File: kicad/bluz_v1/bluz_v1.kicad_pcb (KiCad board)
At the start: 2 copper layers, 24.9 x 14.9 mm, 70 parts, among them J1 USB_B_Micro, J10 Conn, J11 Conn, J12 BTAnt, J2 Conn, J3 Conn, J4 Conn, J5 Conn, J6 Conn, J7 Conn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

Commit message: изменено:      kicad/bluz_v1/bluz_v1.kicad_pcb 	изменено:      kicad/bluz_v1/bluz_v1.kicad_prl 	изменено:      kicad/bluz_v1/bluz_v1.kicad_sch
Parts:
- moved D3 0.78 mm to (80.9, 43.3), turned to 180 degrees
- moved J3 0.16 mm to (82.5, 45.1)
- moved R5 0.09 mm to (82.9, 43.6)
- moved R2 0.09 mm to (81.3, 44.8)
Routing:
- net GND: track 180.8 -> 204.5 mm
- net Net-(D3-Pad1): track 2.48 -> 1.03 mm
- net LED: track 2.35 -> 2.86 mm

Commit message: изменено:      kicad/bluz_v1/bluz_v1.kicad_pcb 	изменено:      kicad/bluz_v1/bluz_v1.kicad_sch 	изменено:      kicad/bluz_v1/fp-info-cache
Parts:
- C12: value .1 -> 10n
- C16: footprint Capacitor_SMD:C_0805_2012Metric -> Capacitor_SMD:C_1206_3216Metric
- C19: footprint Capacitor_SMD:C_0805_2012Metric -> Capacitor_SMD:C_1206_3216Metric; moved to B.Cu
- J11: moved to B.Cu
- moved C19 3.86 mm to (68.0, 40.0), turned to 90 degrees
- moved J11 3.26 mm to (66.3, 38.6)
- moved R14 1.57 mm to (69.7, 38.3), turned to 180 degrees
- moved C16 1.14 mm to (69.9, 41.0)
- moved J10 0.40 mm to (69.6, 42.4)
- moved J6 0.35 mm to (66.2, 49.9)
- moved D5 0.35 mm to (67.7, 41.8)
- moved R15 0.23 mm to (66.2, 38.4)
- moved R13 0.22 mm to (67.6, 38.0)
- moved J12 0.15 mm to (70.6, 39.3)
- moved R16 0.12 mm to (68.2, 39.4)
- moved C9 0.11 mm to (67.3, 39.4)
- moved J3 0.07 mm to (82.6, 45.0)
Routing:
- net GND: track 204.5 -> 208.7 mm
- net Net-(C16-Pad2): track 5.68 -> 6.97 mm
- net /+SiPM: track 2.65 -> 3.01 mm, vias 0 -> 1

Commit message: изменено:      kicad/bluz_v1/bluz_v1.kicad_pcb 	изменено:      kicad/bluz_v1/bluz_v1.kicad_sch 	изменено:      stm32cubeide/BluZ_v1/.cproject 	изменено:      stm32cubeide/BluZ_v1/.mxproject 	изменено:      stm32cubeide/BluZ_v1/.settings/language.settings.xml 	изменено:      stm32cubeide/BluZ_v1/BluZ_v1.ioc 	изменено:      stm32cubeide/BluZ_v1/Core/Inc/app_conf.h 	изменено:      stm32cubeide/BluZ_v1/Core/Inc/main.h 	изменено:      stm32cubeide/BluZ_v1/Core/Inc/stm32wbaxx_it.h 	изменено:      stm32cubeide/BluZ_v1/Core/Src/app_entry.c 	изменено:      stm32cubeide/BluZ_v1/Core/Src/main.c 	изменено:      stm32cubeide/BluZ_v1/Core/Src/stm32wbaxx_hal_msp.c 	изменено:      stm32cubeide/BluZ_v1/Core/Src/stm32wbaxx_it.c
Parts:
- D4: value LTC1661CMS8 -> LTC1662CMS8
- L1: value 47uH -> 10uH
- Q1, Q2, R11, R12: moved to B.Cu
- moved R11 10.8 mm to (83.7, 48.6), turned to 0 degrees
- moved Q1 10.5 mm to (83.5, 50.2)
- moved R12 5.25 mm to (85.0, 45.4), turned to 0 degrees
- moved J9 4.24 mm to (72.3, 47.3)
- moved J4 4.17 mm to (73.3, 48.3)
- moved J5 3.06 mm to (74.5, 47.9)
- moved Q2 2.84 mm to (84.9, 46.9), turned to -90 degrees
- moved L1 2.08 mm to (78.5, 41.8), turned to -90 degrees
- moved J2 1.47 mm to (70.2, 41.5)
- moved C18 1.09 mm to (71.3, 40.9), turned to -90 degrees
- moved R1 0.90 mm to (80.6, 44.7), turned to 90 degrees
- moved J10 0.77 mm to (69.2, 43.0)
- moved BZ1 0.49 mm to (78.3, 48.6)
- moved R2 0.30 mm to (81.6, 44.7)
- moved C11 0.26 mm to (83.1, 42.7)
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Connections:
- D1 pad 15: Sound -> unconnected-(D1-Pad15)
- D1 pad 17: Sync -> unconnected-(D1-Pad17)
- D1 pad 21: unconnected-(D1-Pad21) -> Sync
- D1 pad 6: unconnected-(D1-Pad6) -> LED
- D1 pad 7: LED -> batLev
- D1 pad 8: batLev -> Sound
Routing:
- net GND: track 208.7 -> 203.0 mm
- net Sound: track 4.47 -> 8.57 mm, vias 1 -> 2
- net Sync: track 10.5 -> 14.6 mm
- net /swd: track 1.93 -> 5.88 mm
- net /TxD: track 1.91 -> 5.37 mm
- net Vibro: track 13.9 -> 10.6 mm, vias 1 -> 2
- net Net-(BZ1-Pad2): track 7.86 -> 4.86 mm, vias 0 -> 1
- net /swc: track 2.18 -> 4.97 mm
- net Net-(M1-Pad1): track 1.81 -> 0.00 mm, vias 0 -> 1
- net +BATT: track 37.0 -> 38.6 mm
- net Net-(C23-Pad1): track 4.22 -> 5.44 mm

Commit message: изменено:      kicad/bluz_v1/bluz_v1.kicad_pcb 	изменено:      kicad/bluz_v1/bluz_v1.kicad_prl 	изменено:      kicad/bluz_v1/fp-info-cache
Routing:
- net GND: vias 18 -> 19

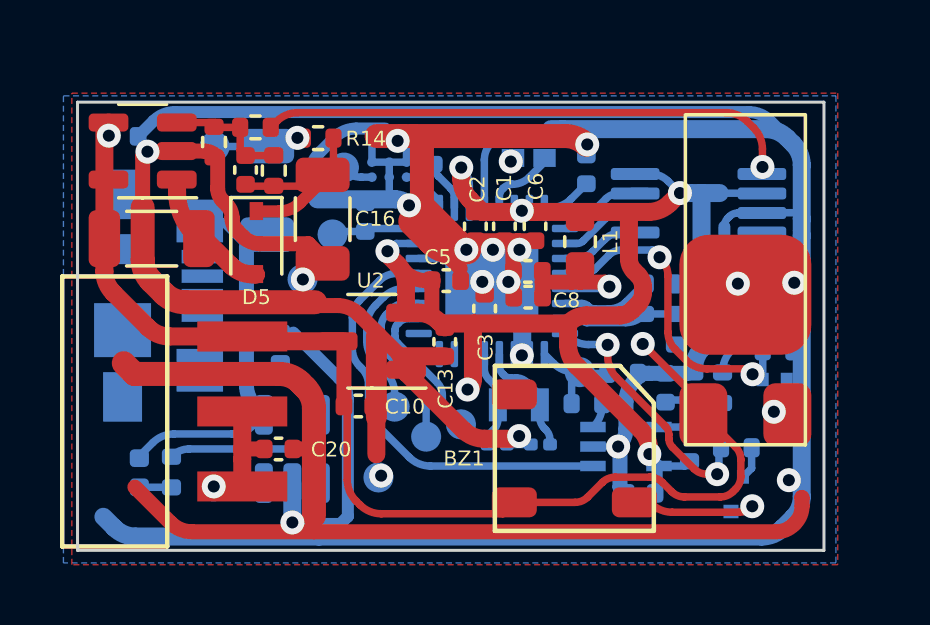
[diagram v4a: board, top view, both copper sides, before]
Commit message: новый файл:    Documents/stm32wba54.jpg 	изменено:      kicad/bluz_v1/bluz_v1.kicad_pcb 	изменено:      kicad/bluz_v1/bluz_v1.kicad_sch 	изменено:      stm32cubeide/BluZ_v1/Core/Src/main.c
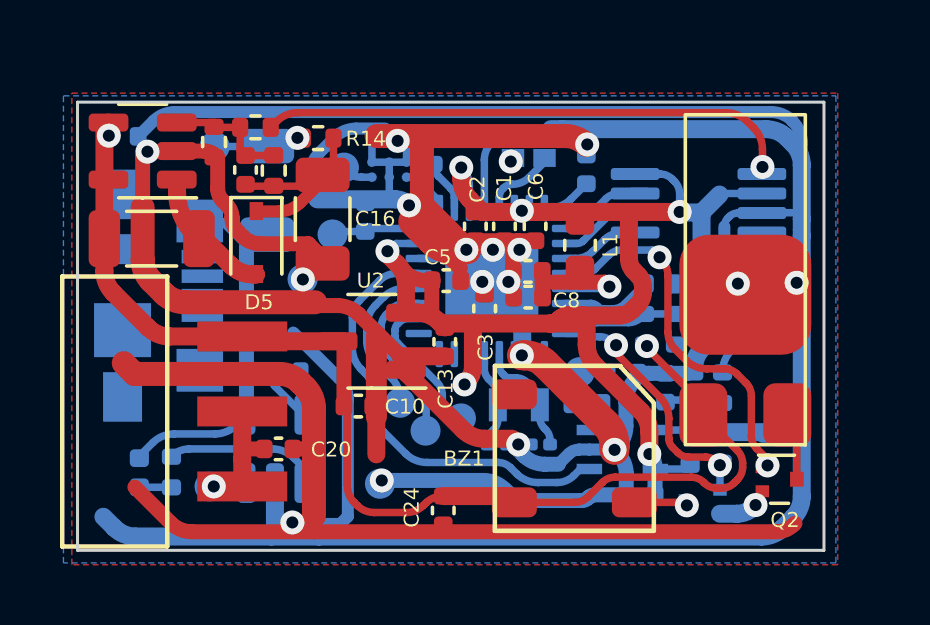
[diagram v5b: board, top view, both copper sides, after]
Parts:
- added C24: 4.7u, Capacitor_SMD:C_0402_1005Metric, F.Cu at (73.9, 50.7)
- L2: value 22uH -> 47uH
- Q2: moved to F.Cu
- R15: value 5.1M -> 4.3M
- moved R12 3.32 mm to (84.7, 48.7), turned to 90 degrees
- moved Q2 2.75 mm to (85.1, 49.7), turned to 0 degrees
- moved Q1 0.97 mm to (82.5, 50.4), turned to 180 degrees
- moved R3 0.82 mm to (68.6, 46.1), turned to 0 degrees
- moved U1 0.58 mm to (68.3, 48.7)
- moved R11 0.47 mm to (83.2, 48.6), turned to 90 degrees
- moved J9 0.22 mm to (72.5, 47.1)
- moved J7 0.22 mm to (71.8, 49.8)
- moved J4 0.20 mm to (73.3, 48.1)
- moved J5 0.20 mm to (74.5, 47.6)
- moved U3 0.16 mm to (79.9, 48.7)
- moved J6 0.14 mm to (66.1, 49.9)
- moved R9 0.12 mm to (82.1, 48.7)
- moved L1 0.12 mm to (78.5, 41.9)
- moved C14 0.06 mm to (80.5, 50.2)
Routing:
- net GND: track 203.0 -> 221.3 mm
- net Net-(BZ1-Pad2): track 4.86 -> 1.70 mm
- net Net-(M1-Pad1): track 0.00 -> 2.28 mm, vias 1 -> 0
- net Vibro: track 10.6 -> 12.5 mm
- net +2V8: track 47.0 -> 48.2 mm
- net Net-(C4-Pad1): track 9.03 -> 8.25 mm
- net Net-(R4-Pad2): track 5.81 -> 5.20 mm
- net /B+: track 4.95 -> 4.37 mm

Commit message: изменено:      kicad/bluz_v1/bluz_v1.kicad_pcb 	изменено:      kicad/bluz_v1/bluz_v1.kicad_sch 	изменено:      stm32cubeide/BluZ_v1/Core/Src/main.c 	изменено:      stm32cubeide/BluZ_v1/Release/Core/Src/subdir.mk 	изменено:      stm32cubeide/BluZ_v1/Release/System/Config/LowPower/peripheral_init.cyclo 	изменено:      stm32cubeide/BluZ_v1/Release/System/Config/LowPower/peripheral_init.su 	изменено:      stm32cubeide/BluZ_v1/Release/System/Interfaces/stm32_lpm_if.cyclo 	изменено:      stm32cubeide/BluZ_v1/Release/System/Interfaces/stm32_lpm_if.su 	изменено:      stm32cubeide/BluZ_v1/Release/System/Interfaces/timer_if.cyclo 	изменено:      stm32cubeide/BluZ_v1/Release/System/Interfaces/timer_if.su 	изменено:      stm32cubeide/BluZ_v1/Release/System/Interfaces/usart_if.cyclo 	изменено:      stm32cubeide/BluZ_v1/Release/System/Interfaces/usart_if.su 	изменено:      stm32cubeide/BluZ_v1/Release/System/Modules/scm.cyclo 	изменено:      stm32cubeide/BluZ_v1/Release/System/Modules/scm.su 	изменено:      stm32cubeide/BluZ_v1/Release/objects.list
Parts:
- moved Q2 0.33 mm to (85.1, 50.0)
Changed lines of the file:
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@@
   )
   (footprint "My-library:SOT-723" (layer "F.Cu")
-    (at 85.1 49.68)
+    (at 85.11 50.01)
     (descr "http://toshiba.semicon-storage.com/info/docget.jsp?did=5879&prodName=RN1104MFV")
     (tags "sot 723")
@@
   (segment (start 78.44 46.11) (end 78.276714 46.11) (width 0.25) (layer "B.Cu") (net 11))
   (arc (start 77.569607 45.817107) (mid 77.89403 46.03388) (end 78.276714 46.11) (width 0.25) (layer "B.Cu") (net 11))
+  (segment (start 83.685736 46.175736) (end 83.984264 46.474264) (width 0.25) (layer "F.Cu") (net 12))
+  (segment (start 81.614314 45.344314) (end 81.977107 45.707107) (width 0.25) (layer "F.Cu") (net 12))
   (segment (start 81.1 42.28) (end 81.145685 42.325685) (width 0.25) (layer "F.Cu") (net 12))
-  (segment (start 84.16 46.898528) (end 84.16 48.231472) (width 0.25) (layer "F.Cu") (net 12))
-  (segment (start 81.614314 45.344314) (end 81.977107 45.707107) (width 0.25) (layer "F.Cu") (net 12))
-  (segment (start 84.7 49.02) (end 84.7 49.22) (width 0.25) (layer "F.Cu") (net 12))
-  (segment (start 84.335736 48.655736) (end 84.7 49.02) (width 0.25) (layer "F.Cu") (net 12))
+  (segment (start 84.535 49.61) (end 84.535 49.385) (width 0.25) (layer "F.Cu") (net 12))
+  (segment (start 84.452893 48.792893) (end 84.7 49.04) (width 0.25) (layer "F.Cu") (net 12))
+  (segment (start 82.684214 46) (end 83.261472 46) (width 0.25) (layer "F.Cu") (net 12))
+  (segment (start 84.535 49.385) (end 84.7 49.22) (width 0.25) (layer "F.Cu") (net 12))
+  (segment (start 84.16 46.898528) (end 84.16 48.085786) (width 0.25) (layer "F.Cu") (net 12))
+  (segment (start 84.7 49.04) (end 84.7 49.22) (width 0.25) (layer "F.Cu") (net 12))
   (segment (start 81.38 42.891371) (end 81.38 44.778629) (width 0.25) (layer "F.Cu") (net 12))
-  (segment (start 83.685736 46.175736) (end 83.984264 46.474264) (width 0.25) (layer "F.Cu") (net 12))
-  (segment (start 82.684214 46) (end 83.261472 46) (width 0.25) (layer "F.Cu") (net 12))
   (via (at 84.7 49.22) (size 0.8) (drill 0.4) (layers "F.Cu" "B.Cu") (net 12))
   (via (at 81.1 42.28) (size 0.8) (drill 0.4) (layers "F.Cu" "B.Cu") (free) (net 12))
-  (arc (start 84.335736 48.655736) (mid 84.205672 48.461082) (end 84.16 48.231472) (width 0.25) (layer "F.Cu") (net 12))
+  (arc (start 83.261472 46) (mid 83.491082 46.045672) (end 83.685736 46.175736) (width 0.25) (layer "F.Cu") (net 12))
+  (arc (start 84.452893 48.792893) (mid 84.23612 48.46847) (end 84.16 48.085786) (width 0.25) (layer "F.Cu") (net 12))
   (arc (start 81.145685 42.325685) (mid 81.319103 42.585224) (end 81.38 42.891371) (width 0.25) (layer "F.Cu") (net 12))
   (arc (start 81.38 44.778629) (mid 81.440896 45.084775) (end 81.614314 45.344314) (width 0.25) (layer "F.Cu") (net 12))
   (arc (start 83.984264 46.474264) (mid 84.114328 46.668918) (end 84.16 46.898528) (width 0.25) (layer "F.Cu") (net 12))
-  (arc (start 83.261472 46) (mid 83.491082 46.045672) (end 83.685736 46.175736) (width 0.25) (layer "F.Cu") (net 12))
   (arc (start 81.977107 45.707107) (mid 82.301531 45.92388) (end 82.684214 46) (width 0.25) (layer "F.Cu") (net 12))
   (segment (start 77.9475 42.82) (end 78.592893 42.82) (width 0.25) (layer "B.Cu") (net 12))
@@
   (arc (start 78.697157 44.32) (mid 78.773694 44.335224) (end 78.838579 44.378579) (width 0.25) (layer "B.Cu") (net 37))
   (arc (start 80.485736 44.284264) (mid 80.291082 44.414328) (end 80.061472 44.46) (width 0.25) (layer "B.Cu") (net 37))
-  (segment (start 85.675 47.845) (end 85.36 47.53) (width 0.25) (layer "F.Cu") (net 38))
-  (segment (start 85.675 49.68) (end 85.675 47.845) (width 0.25) (layer "F.Cu") (net 38))
+  (segment (start 85.685 47.855) (end 85.36 47.53) (width 0.25) (layer "F.Cu") (net 38))
+  (segment (start 85.685 50.01) (end 85.685 47.855) (width 0.25) (layer "F.Cu") (net 38))
   (segment (start 65.603287 41.518287) (end 65.745 41.66) (width 0.6) (layer "F.Cu") (net 39))
   (segment (start 65.0175 39.75) (end 65.0175 40.104073) (width 0.6) (layer "F.Cu") (net 39))

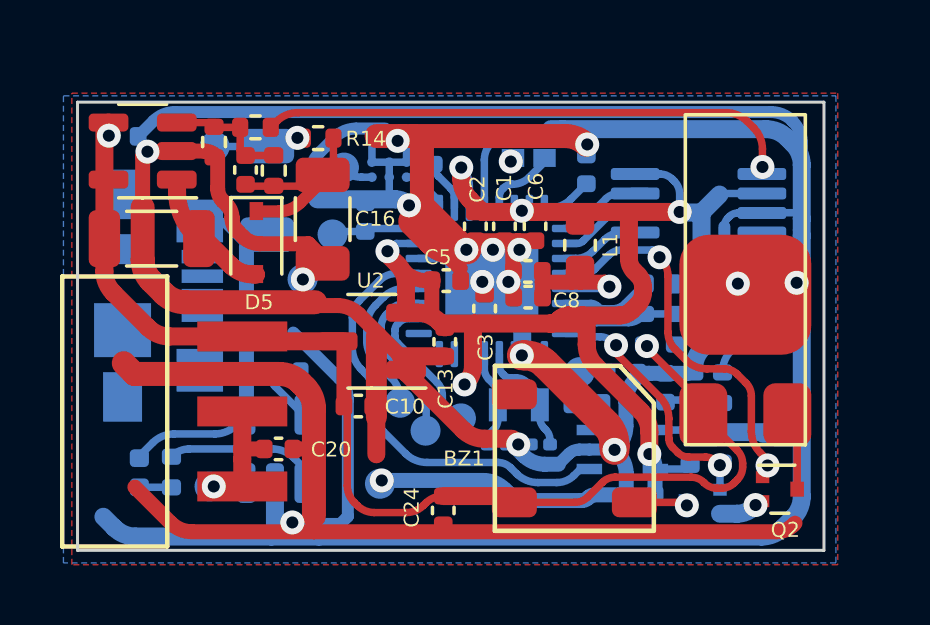
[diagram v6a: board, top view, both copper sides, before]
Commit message: новый файл:    Documents/DFT.ods 	изменено:      FreeCAD/BluZ_case.FCStd 	изменено:      FreeCAD/BluZ_case.stl 	изменено:      kicad/bluz_v1/bluz_v1.kicad_pcb 	изменено:      kicad/bluz_v1/bluz_v1.kicad_sch
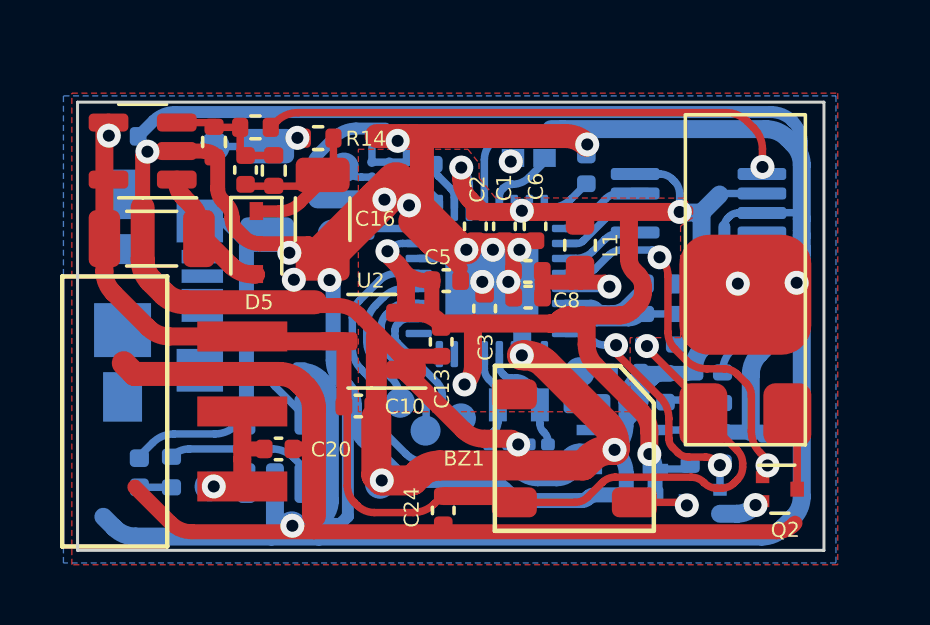
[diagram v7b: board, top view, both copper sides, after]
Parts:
- moved J10 8.25 mm to (68.8, 51.2)
- moved C13 0.12 mm to (73.8, 45.1)
- moved C21 0.08 mm to (75.8, 48.5)
- moved R6 0.08 mm to (80.0, 46.1)
- moved C22 0.07 mm to (77.1, 48.5)
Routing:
- net GND: track 221.3 -> 253.9 mm, vias 19 -> 22
- added copper zone on F.Cu, net +2V8
